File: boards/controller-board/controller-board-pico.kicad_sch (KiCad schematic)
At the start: 59 parts, among them J1 12V, J2 Conn_01x02, J3 Conn_01x02, J4 Conn_01x02, J5 0470531000, J6 Phoenix 1935161, Q1 PMV45EN, Q2 Goford_G11S_20V_11A, U1 XIAO-RP2040-SMD, U2 ADS1015IRUGR, U5 MCP4728

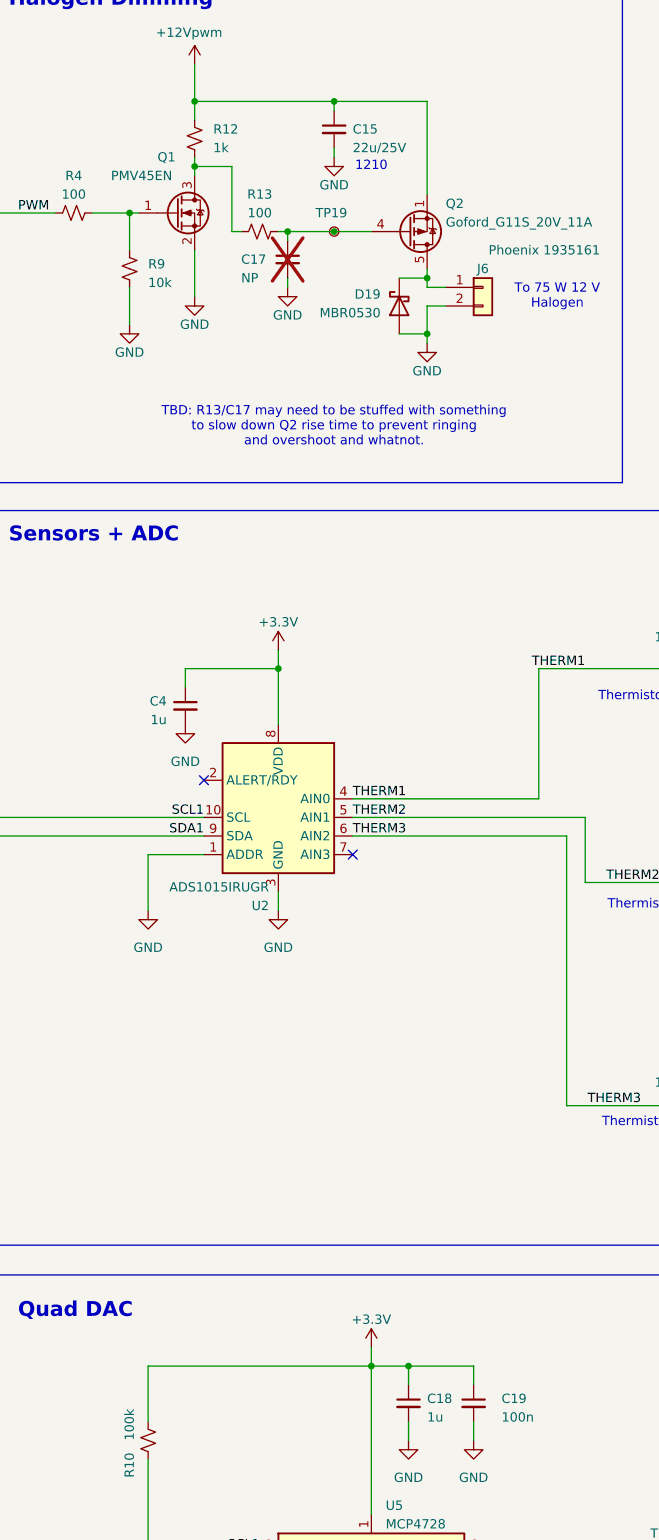
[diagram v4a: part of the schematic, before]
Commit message: Clean up library links, fix ERC errors, dix DRC errors, add more 3D models, and add makefile and readme.
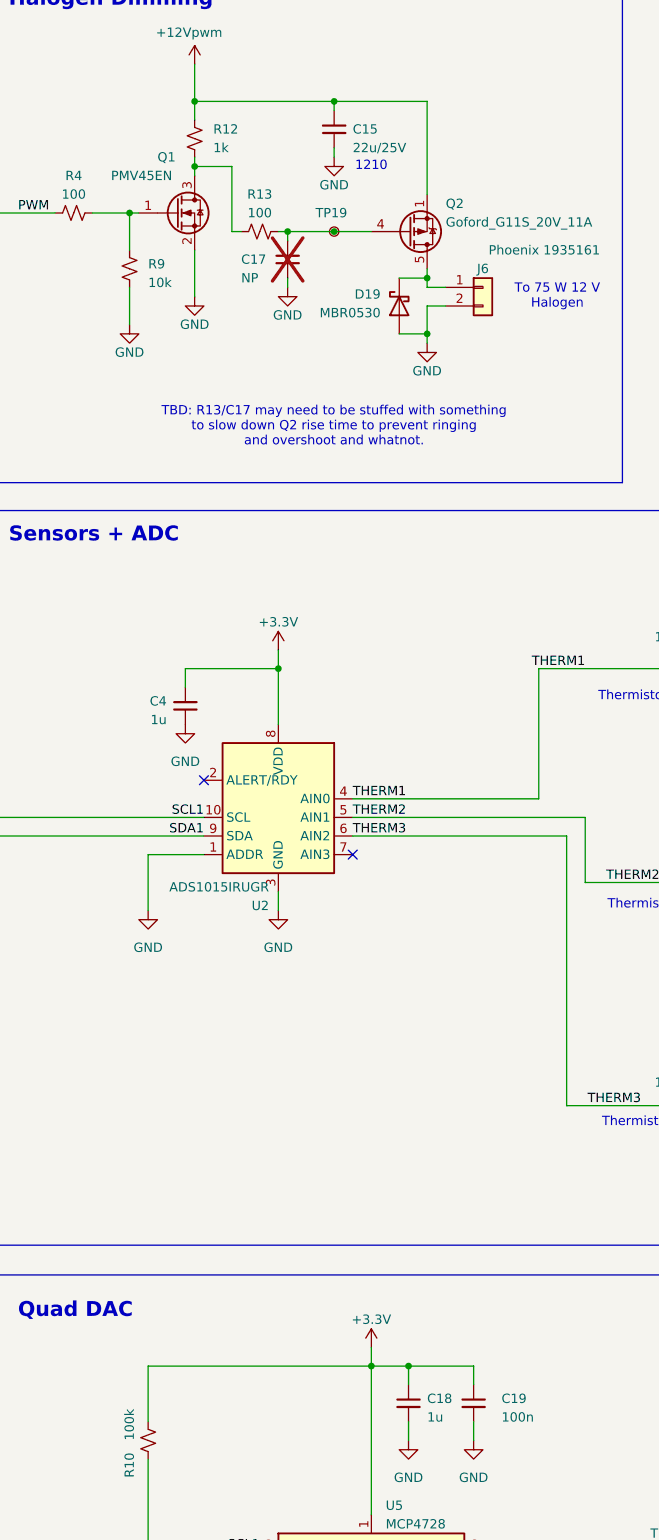
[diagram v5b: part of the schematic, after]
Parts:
- C15, C17, C18, C19, C4, D19, F1, F2, F3, F4, J2, J3, J4, J6, R1, R10, R12, R13, R2, R3, R4, R48, R49, R50, R51, R7, R8, R9, U2, U5: DIS (none) -> DigiKey; Distributor DigiKey -> (none)
- J1: footprint controller_brd_footprints:CONN_6P_RECPT -> controller_brd:CONN_6P_RECPT; DIS (none) -> Digikey; DURL https://www.digikey.com/en/products/detail/molex/0015247061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 -> (none); Distributor Digikey -> (none)
- J5: Distrubuter Link https://www.digikey.com/en/products/detail/molex/0470531000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 -> (none); Manufacturer Molex -> (none)
- Q1: symbol Device:Q_NMOS_GSD -> Transistor_FET:Q_NMOS_GSD; DIS (none) -> DigiKey; Distributor DigiKey -> (none)
- Q2: footprint Package_SO:SOP-8_3.9x4.9mm_P1.27mm -> Package_SO:SOP-8_3.76x4.96mm_P1.27mm; DIS (none) -> DigiKey; Distributor DigiKey -> (none)
- U1: footprint Seeed_Studio_XIAO_Series:XIAO-RP2040-SMD -> controller_brd:XIAO-RP2040-SMD; DIS (none) -> Digikey; DURL https://www.digikey.com/en/products/detail/seeed-technology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 -> (none); Distributor Digikey -> (none)

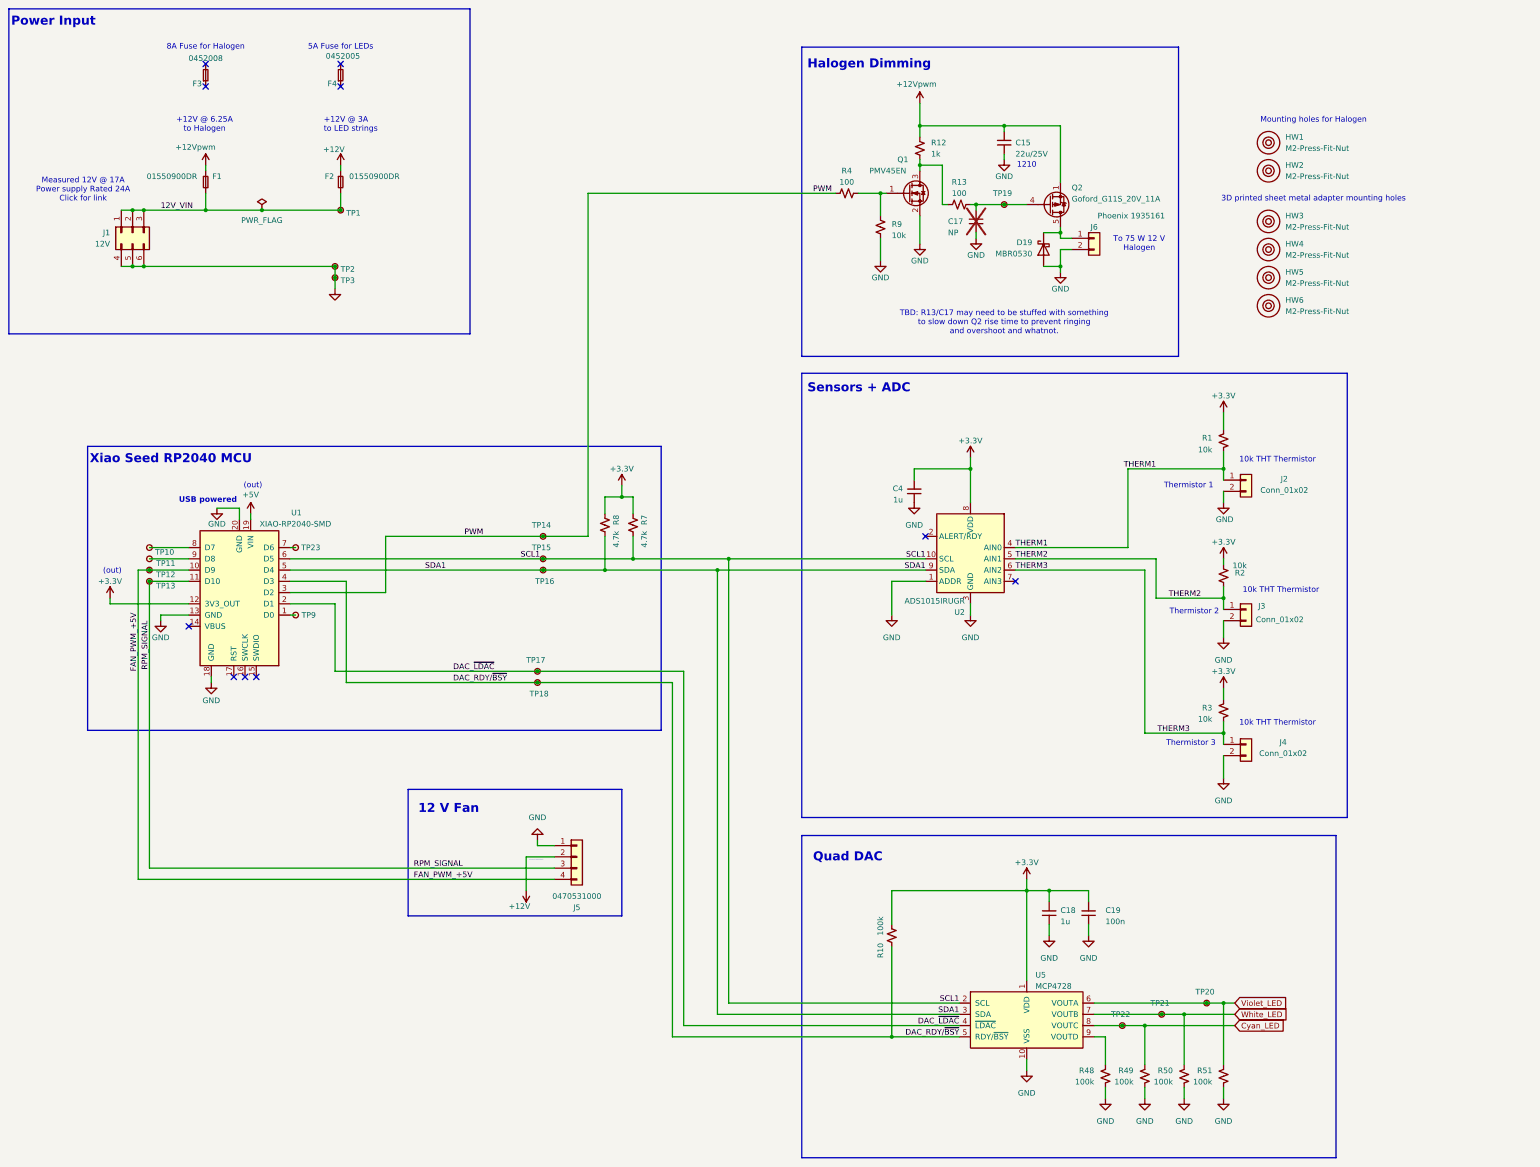
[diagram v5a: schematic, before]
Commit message: Added LED test points. Added heatsinks and notes on thermal paste. Cleaned up bottom traces with new LED test points. Some hierarchical labels, some cleanup of schematic and layout. Builds.
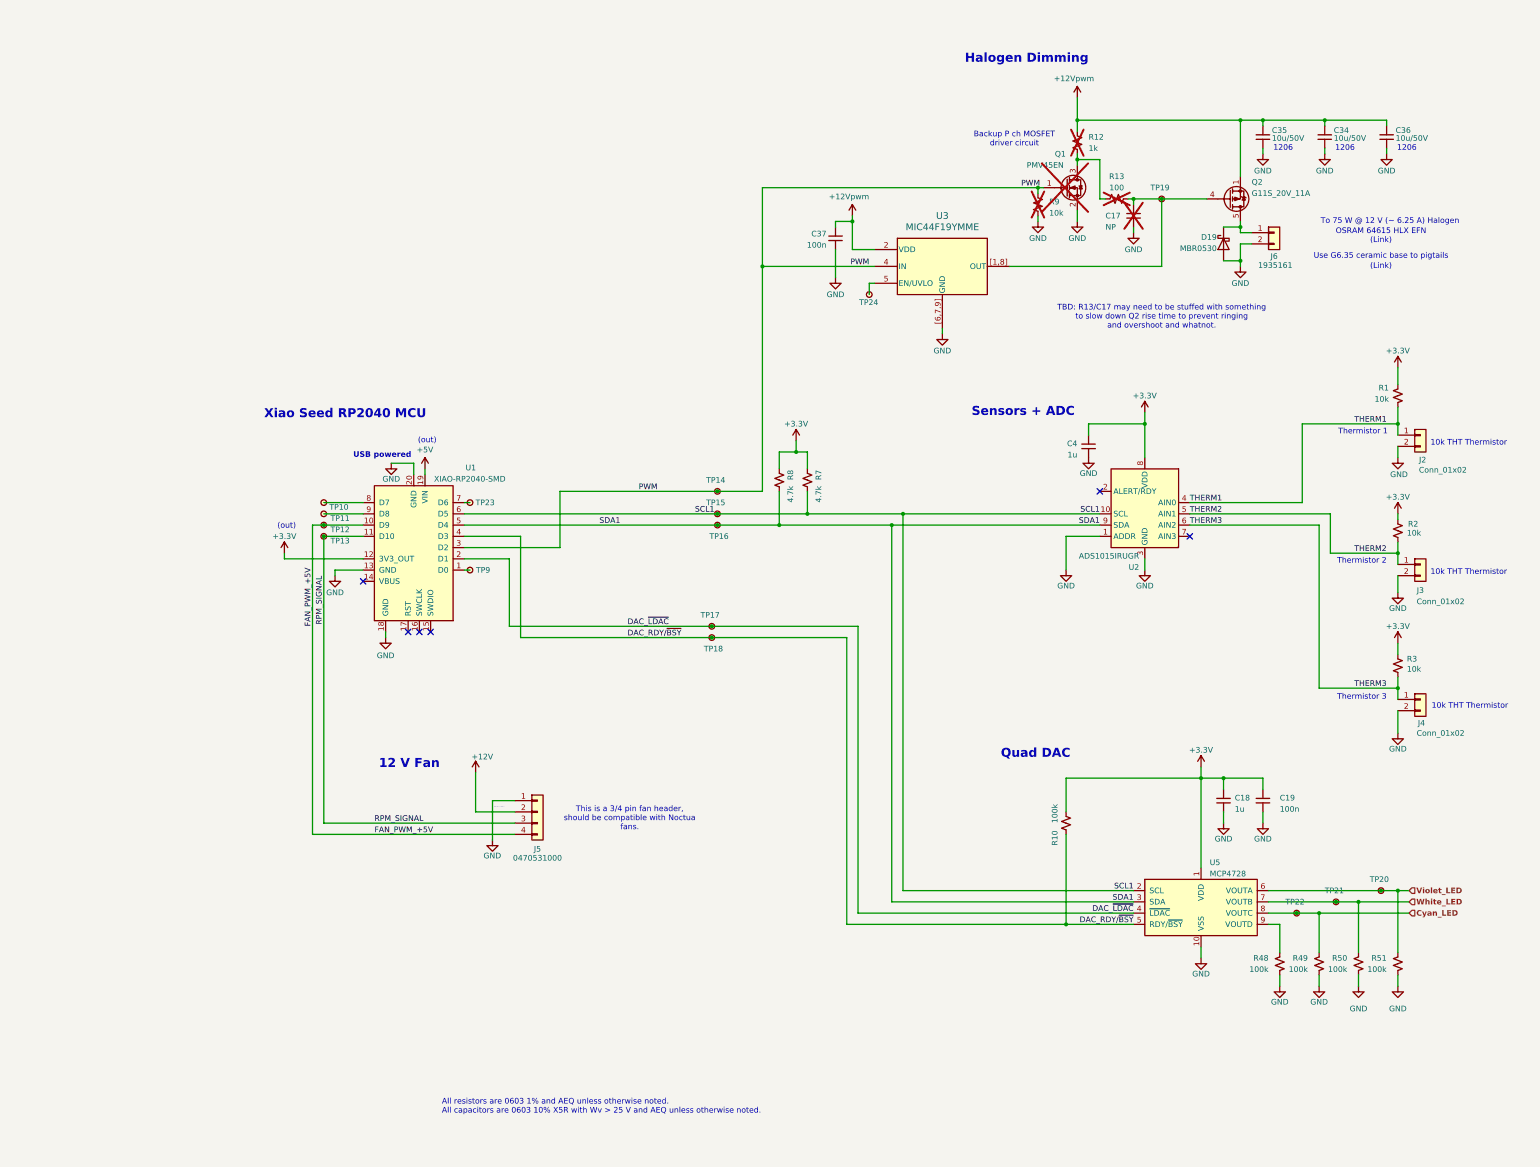
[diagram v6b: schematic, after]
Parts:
- removed C15: 22u/25V, Capacitor_SMD:C_1210_3225Metric, symbol Device:C_Small
- removed F1, F2: 01550900DR, Fuse:Fuseholder_Littelfuse_Nano2_154x, symbol Device:Fuse_Small
- removed F3: 0452008, symbol Device:Fuse_Small
- removed F4: 0452005, Fuse:Fuseholder_Littelfuse_Nano2_154x, symbol Device:Fuse_Small
- removed HW1, HW2, HW3, HW4, HW5, HW6: M2-Press-Fit-Nut, oresat-misc:M2-Press-Fit-Nut, symbol oresat-misc:M2-Press-Fit-Nut
- removed J1: 12V, controller_brd:CONN_6P_RECPT, symbol Connector_Generic:Conn_02x03_Top_Bottom
- removed R4: 100, oresat-passives:0603-C-NOSILK, symbol Device:R_Small_US
- removed TP1, TP2, TP3: TestPoint-MinTH, oresat-misc:TestPoint-MinTH, symbol oresat-misc:TestPoint-MinTH
- added C34, C35, C36: 10u/50V, oresat-passives:1206-C, symbol Device:C_Small
- added C37: 100n, oresat-passives:0603-C-NOSILK, symbol Device:C_Small
- added TP24: TestPoint-MinTH, oresat-misc:TestPoint-MinTH, symbol oresat-misc:TestPoint-MinTH
- added U3: MIC44F19YMME, oresat-ics:MSOP-8_MME_MCL, symbol oresat-ics:MIC44F19YMME
- C19: DPN 490-6328-1-ND -> 399-6856-1-ND; MFR Murata Electronics -> KEMET; MPN GRM155R71C104KA88J -> C0603C104K5RACAUTO
- J5: DIS (none) -> DigiKey; MFR (none) -> Molex
- J6: value Phoenix 1935161 -> 1935161
- Q1: now not fitted
- Q2: value Goford_G11S_20V_11A -> G11S_20V_11A
- R1, R2, R3: DPN 311-10.0KHRCT-ND -> RMCF0603FT10K0CT-ND; MFR Yageo -> Stackpole Electronics; MPN RC0603FR-0710KL -> RMCF0603FT10K0
- R10, R48, R49, R50, R51: DPN 311-100KHRCT-ND -> RMCF0603FT100KCT-ND; MFR Yageo -> Stackpole Electronics; MPN RC0603FR-07100KL -> RMCF0603FT100K
- R12: DPN 311-1.00KHRCT-ND -> RMCF0603FT2K70CT-ND; MFR Yageo -> Stackpole Electronics; MPN RC0603FR-071KL -> RMCF0603FT1K00; now not fitted
- R13: DPN 311-100GRCT-ND -> RMCF0603FT100RCT-ND; MFR Yageo -> Stackpole Electronics; MPN RC0603JR-07100RL -> RMCF0603FT100R; now not fitted
- R7, R8: DPN 311-4.70KHRCT-ND -> RMCF0603FT4K70CT-ND; MFR Yageo -> Stackpole Electronics; MPN RC0603FR-074K7L -> RMCF0603FT4K70
- R9: DPN 311-10.0KHRCT-ND -> RMCF0603FT10K0CT-ND; MFR Yageo -> Stackpole Electronics; MPN RC0603FR-0710KL -> RMCF0603FT10K0; now not fitted
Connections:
- net +12Vpwm: now also C34.1, C35.1, C36.1, C37.1, U3.2 (VDD)
- net GND: now also C34.2, C35.2, C36.2, C37.2, U3.[6,7,9] (GND)
- net PWM: now also Q1.1 (G), R9.1, U3.4 (IN)
- net at C17.1, Q2.4 (G), R13.2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: now also U3.[1,8] (OUT)
- new net: TP24.1, U3.5 (EN/UVLO)
- no-connect marks 10 -> 6
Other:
- note added: "(Link)"
- note added: "1206"
- note added: "All resistors are 0603 1% and AEQ unless otherwise noted. All capacitors are 0603 10% X5R with Wv > 25 V and AEQ unless otherwise noted."
- note added: "Backup P ch MOSFET driver circuit"
- note added: "Nope, not on my watch!!!"
- note added: "OSRAM 64615 HLX EFN"
- note added: "This is a 3/4 pin fan header, should be compatible with Noctua fans."
- note added: "To 75 W @ 12 V (~ 6.25 A) Halogen"
- note added: "Use G6.35 ceramic base to pigtails"
- note removed: "+12V @ 3A to LED strings"
- note removed: "+12V @ 6.25A to Halogen"
- note removed: "1210"
- note removed: "3D printed sheet metal adapter mounting holes"
- note removed: "5A Fuse for LEDs"
- note removed: "8A Fuse for Halogen"
- note removed: "Measured 12V @ 17A Power supply Rated 24A Click for link"
- note removed: "Mounting holes for Halogen"
- note removed: "Power Input"
- note removed: "To 75 W 12 V Halogen"
- note removed: "just a weee bit of electrical terrorism"
- moved on the sheet: C17, C18, C19, C4, D19, J2, J3, J4, J5, J6, Q2, R1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

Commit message: v2.1 out the door! Fixed BOM, last minute double checks
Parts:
- added TH1, TH2, TH3: NXFT15XV103FEAB050, symbol Device:Thermistor
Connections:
- no-connect marks 6 -> 12
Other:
- note added: "Ext. Thermistors"
